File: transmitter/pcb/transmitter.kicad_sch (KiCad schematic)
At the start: 14 parts, among them U1 AMS1117-3.3, U2 MOUDLE-SEEEDUINO-XIAO-ESP32C3

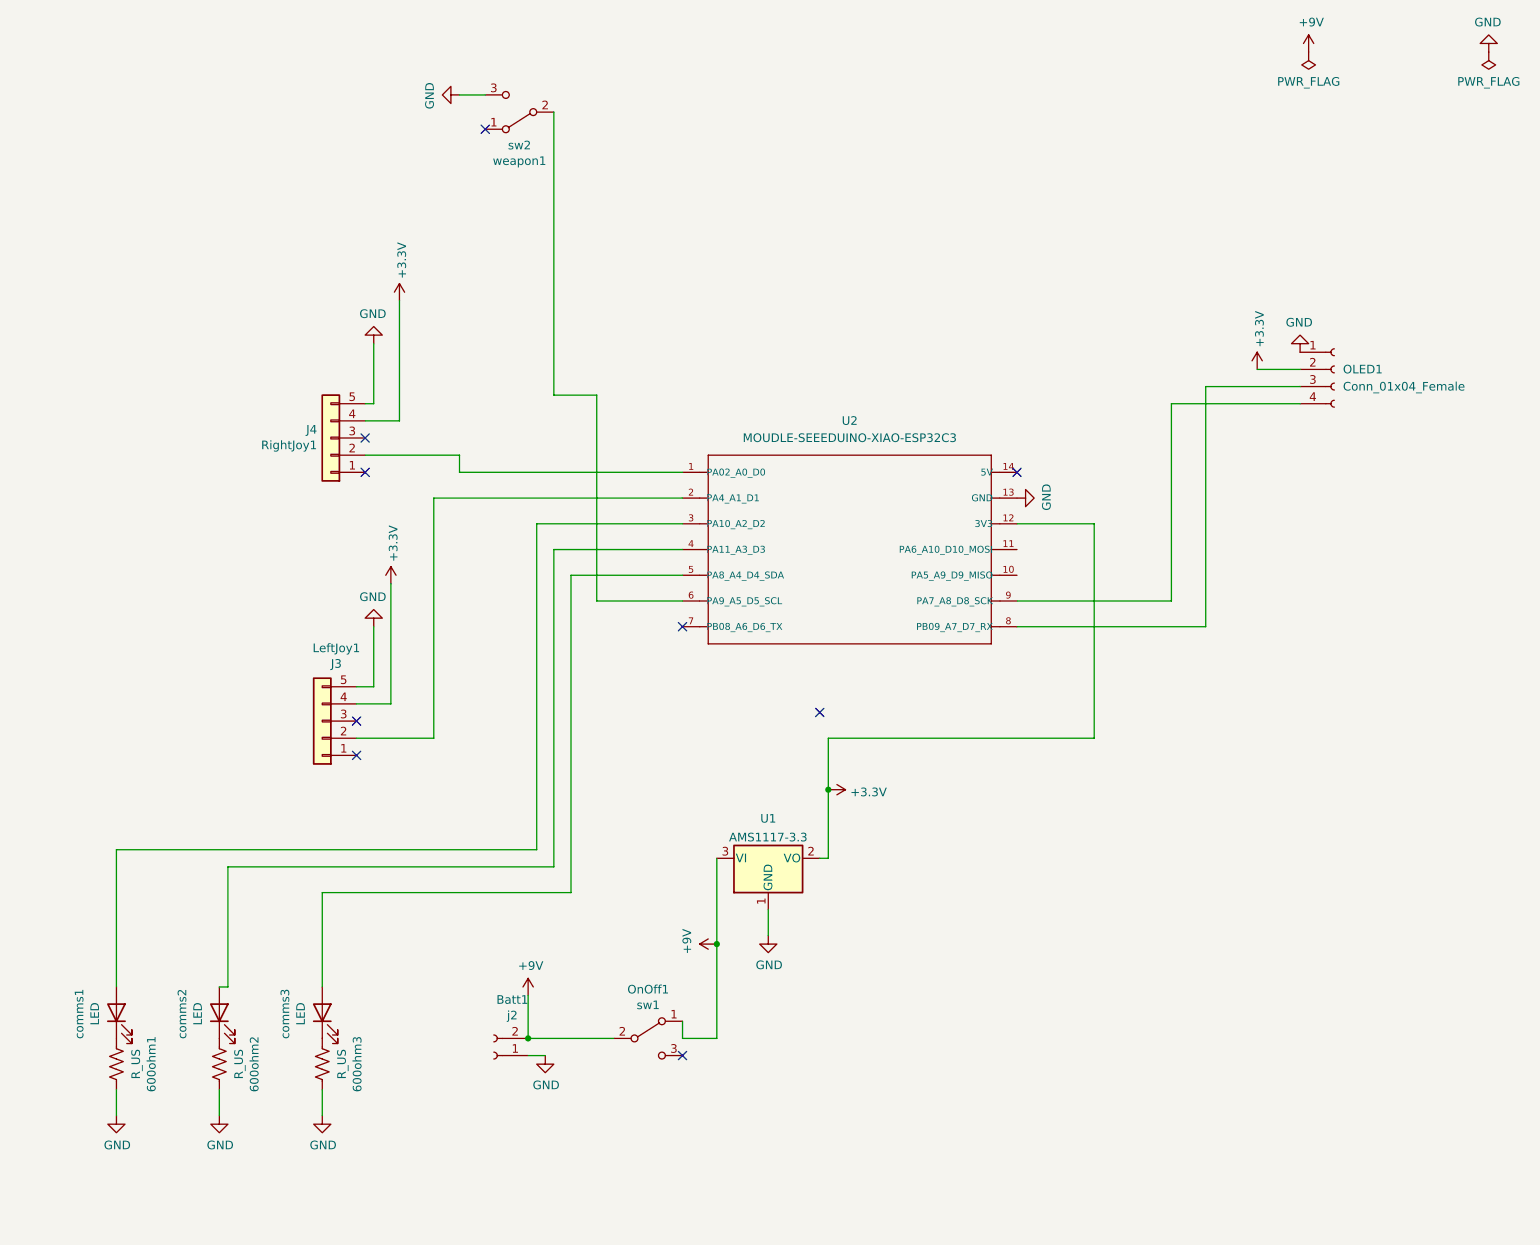
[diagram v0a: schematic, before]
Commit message: Ready for Review
added trigger switches and joysticks

schematic is probably fine, but all of the route tracing needs to be redone

adjusted transmitter for ps4 geometry

added footprints

added passives adjusted pin assignment

ready for review
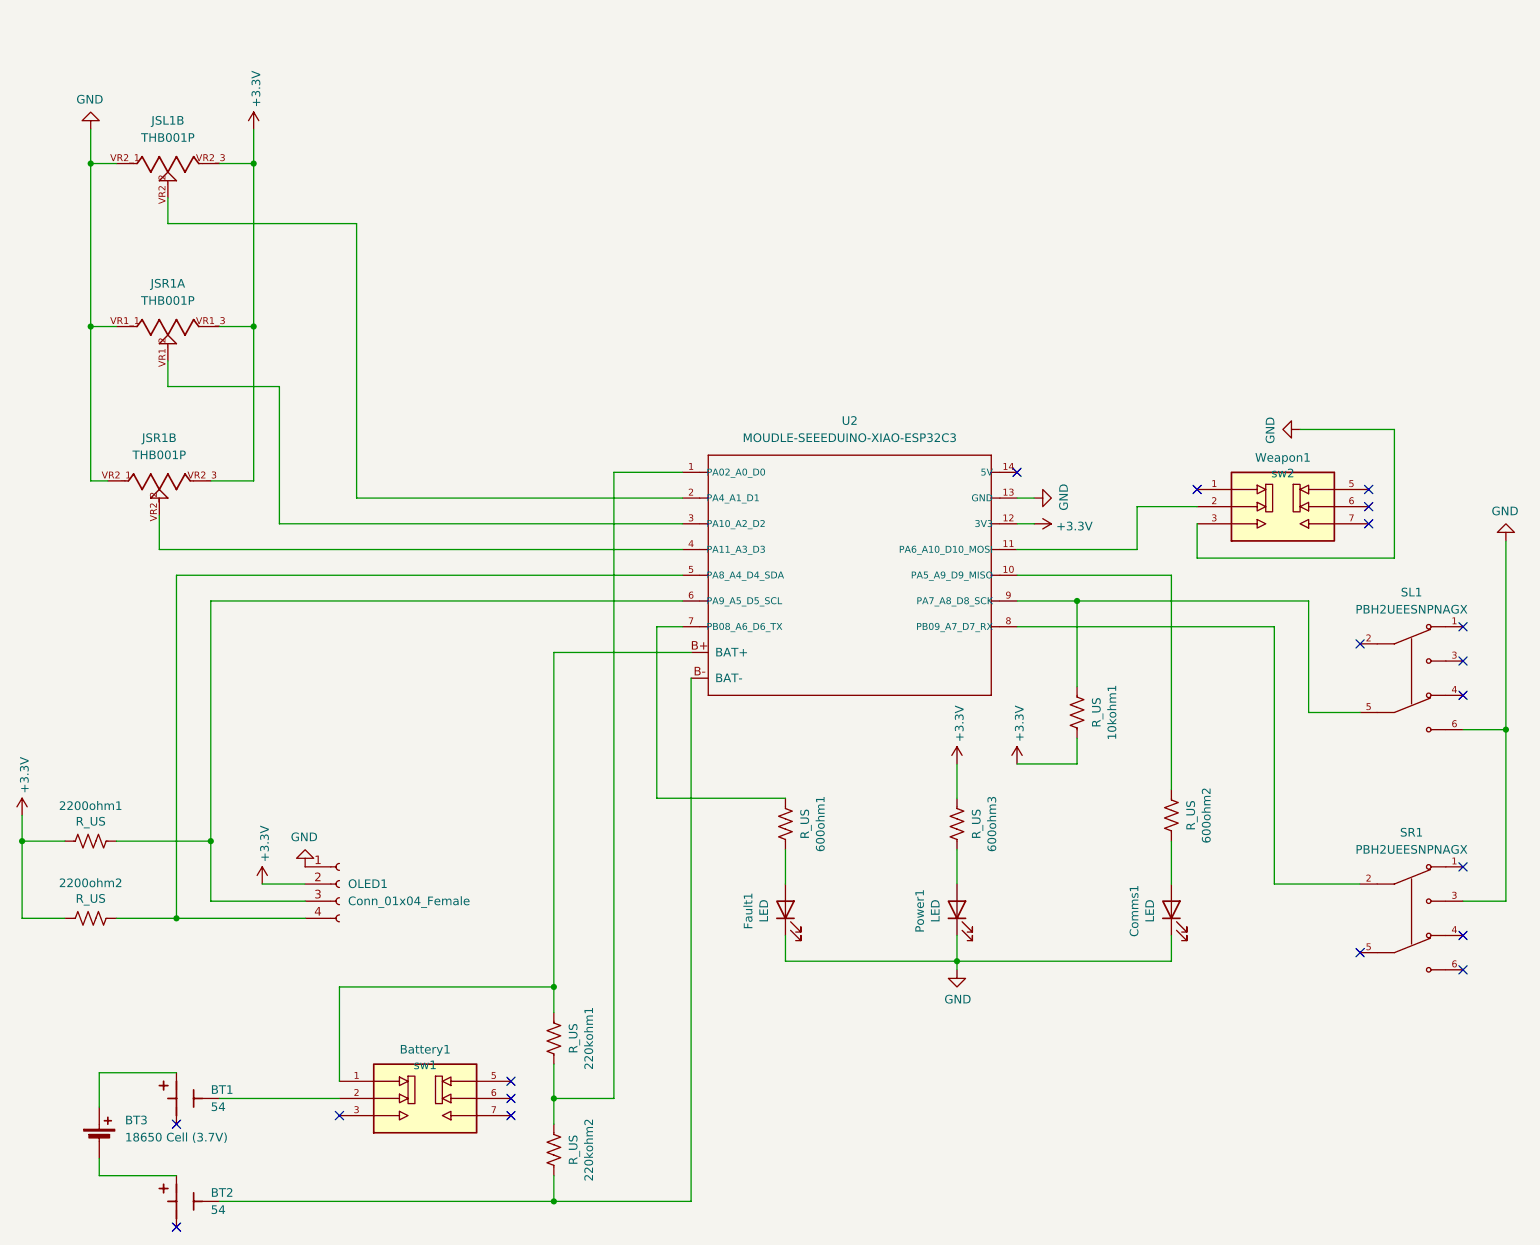
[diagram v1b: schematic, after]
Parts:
- removed Batt1: j2, Connector_PinSocket_2.54mm:PinSocket_1x02_P2.54mm_Vertical, symbol Connector:Conn_01x02_Female
- removed LeftJoy1: J3, Connector_PinSocket_2.54mm:PinSocket_1x05_P2.54mm_Vertical, symbol Connector_Generic:Conn_01x05
- removed RightJoy1: J4, Connector_PinSocket_2.54mm:PinSocket_1x05_P2.54mm_Vertical, symbol Connector_Generic:Conn_01x05
- removed U1: AMS1117-3.3, Package_TO_SOT_SMD:SOT-223-3_TabPin2, symbol Regulator_Linear:AMS1117-3.3
- added 10kohm1, 2200ohm1, 2200ohm2, 220kohm1, 220kohm2: R_US, Resistor_SMD:R_0805_2012Metric_Pad1.20x1.40mm_HandSolder, symbol Device:R_US
- added BT1, BT2: 54, SnapEDA Library:BAT_54, symbol KEYSTONE_54:54
- added BT3: 18650 Cell (3.7V), symbol Device:Battery_Cell
- added JSL1, JSR1: THB001P, CNK_THB001P, symbol THB001P:THB001P
- added SL1, SR1: PBH2UEESNPNAGX, SW_PBH2UEESNPNAGX, symbol PBH2UEESNPNAGX:PBH2UEESNPNAGX
- Battery1: renamed from OnOff1; footprint Connector_PinSocket_2.54mm:PinSocket_1x03_P2.54mm_Vertical -> SnapEDA Library:SW_JS202011JCQN; symbol Switch:SW_SPDT -> JS202011JCQN:JS202011JCQN; MANUFACTURER (none) -> C&K; MAXIMUM_PACKAGE_HEIGHT (none) -> 5.6 mm; PARTREV (none) -> 11 Nov 19; STANDARD (none) -> Manufacturer Recommendations
- Weapon1: renamed from weapon1; footprint Connector_PinSocket_2.54mm:PinSocket_1x03_P2.54mm_Vertical -> SnapEDA Library:SW_JS202011JCQN; symbol Switch:SW_SPDT -> JS202011JCQN:JS202011JCQN; MANUFACTURER (none) -> C&K; MAXIMUM_PACKAGE_HEIGHT (none) -> 5.6 mm; PARTREV (none) -> 11 Nov 19; STANDARD (none) -> Manufacturer Recommendations
- renumbered comms2 to Comms1, comms1 to Fault1, comms3 to Power1
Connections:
- net +3.3V: now also 600ohm3.2, 10kohm1.1, 2200ohm1.2, 2200ohm2.2, JSL1.VR2_3, JSR1.VR1_3, JSR1.VR2_3
- net GND: now also Comms1.1 (K), Fault1.1 (K), Power1.1 (K), JSL1.VR2_1, JSR1.VR1_1, JSR1.VR2_1, SL1.6, SR1.3; no longer 600ohm1.1, 600ohm2.1, 600ohm3.1
- net at U2.2 (PA4_A1_D1): now also JSL1.VR2_2
- net at U2.1 (PA02_A0_D0): now also 220kohm1.1, 220kohm2.2
- net at Weapon1.2: now also U2.11 (PA6_A10_D10_MOSI); no longer U2.6 (PA9_A5_D5_SCL)
- net at U2.8 (PB09_A7_D7_RX): now also SR1.2; no longer OLED1.3 (Pin_3)
- net at OLED1.4 (Pin_4): now also U2.5 (PA8_A4_D4_SDA), 2200ohm2.1; no longer U2.9 (PA7_A8_D8_SCK)
- net at 600ohm2.2: now also U2.10 (PA5_A9_D9_MISO); no longer Comms1.1 (K)
- net at Comms1.2 (A): now also 600ohm2.1; no longer U2.4 (PA11_A3_D3)
- net at Power1.2 (A): now also 600ohm3.1; no longer U2.5 (PA8_A4_D4_SDA)
- net at U2.3 (PA10_A2_D2): now also JSR1.VR1_2; no longer Fault1.2 (A)
- net at U2.7 (PB08_A6_D6_TX): now also 600ohm1.2
- net +9V: no longer names the net of Battery1.1
- net +9V: now also U2.B+ (BAT+), 220kohm1.2; no longer Battery1.2 (B)
- new net: BT1.1_3, Battery1.2
- new net: 2200ohm1.1, OLED1.3 (Pin_3), U2.6 (PA9_A5_D5_SCL)
- new net: BT2.1_1, BT3.2 (-)
- new net: 220kohm2.1, BT2.1_3, U2.B- (BAT-)
- new net: 10kohm1.2, SL1.5, U2.9 (PA7_A8_D8_SCK)
- new net: JSR1.VR2_2, U2.4 (PA11_A3_D3)
- new net: BT1.1_1, BT3.1 (+)
- new net: 600ohm1.1, Fault1.2 (A)
- no-connect marks 9 -> 19
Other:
- moved on the sheet: 600ohm1, 600ohm2, 600ohm3, Comms1, Fault1, OLED1, Power1

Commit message: V3 transmitter PCB
* moar resistor labels!
* re-routed analog inputs for joysticks, swapped a joystick sideways input for joystick click
* fixed improper use of a digital IO that needs to be an input
* battery connections are a through-pad...very excited to see if this works!
* spaced battery clips apart an extra 2.5mm
* added extra resistance to bring joystick voltages back into 2.5V range
* added some extra cutouts so we can use a 4 pole trigger button instead of 2 pole because its cheaper (momentary version)
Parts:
- removed unit 1 of JSR1
- added 3300ohm1, 3300ohm2: R_US, Resistor_SMD:R_0805_2012Metric_Pad1.20x1.40mm_HandSolder, symbol Device:R_US
- added unit 3 of JSR1
- renumbered 600ohm3 to 620ohm3, 600ohm1 to 62ohm1, 600ohm2 to 62ohm2
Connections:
- net +3.3V: now also 3300ohm1.1, 3300ohm2.1; no longer JSL1.VR2_3, JSR1.VR2_3
- net GND: now also JSR1.C, JSR1.D
- net at SR1.2: now also 10kohm1.2, U2.9 (PA7_A8_D8_SCK); no longer U2.8 (PB09_A7_D7_RX)
- net at U2.3 (PA10_A2_D2): now also JSR1.VR2_2
- net at U2.10 (PA5_A9_D9_MISO): now also SL1.5; no longer 62ohm2.2
- net at U2.4 (PA11_A3_D3): now also JSR1.A, JSR1.B; no longer JSR1.VR2_2
- new net: 3300ohm2.2, JSR1.VR2_3
- new net: 3300ohm1.2, JSL1.VR2_3
- new net: 62ohm2.2, U2.8 (PB09_A7_D7_RX)
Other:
- moved on the sheet: JSR1B
